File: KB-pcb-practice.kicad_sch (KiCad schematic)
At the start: 12 parts

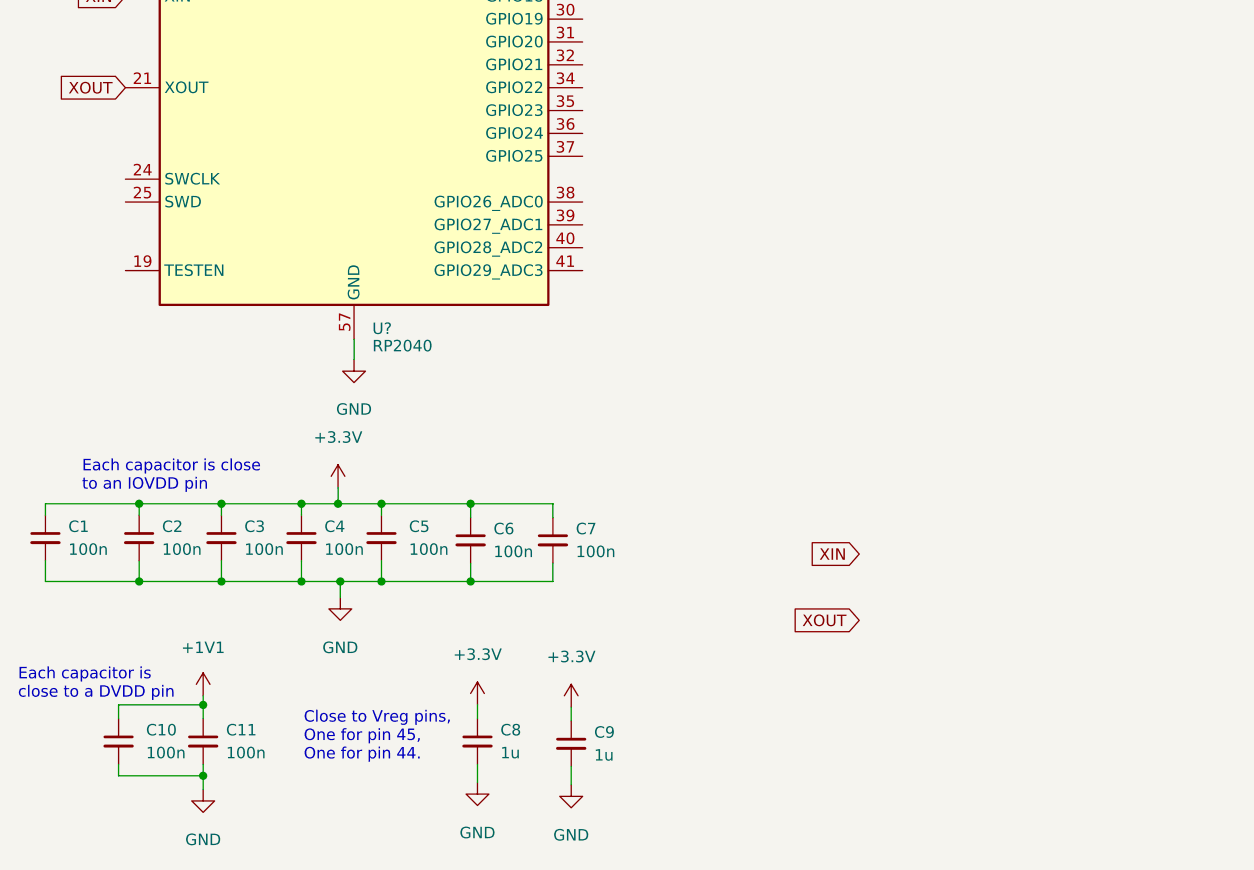
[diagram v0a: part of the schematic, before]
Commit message: Added Clock Circuit to Sch
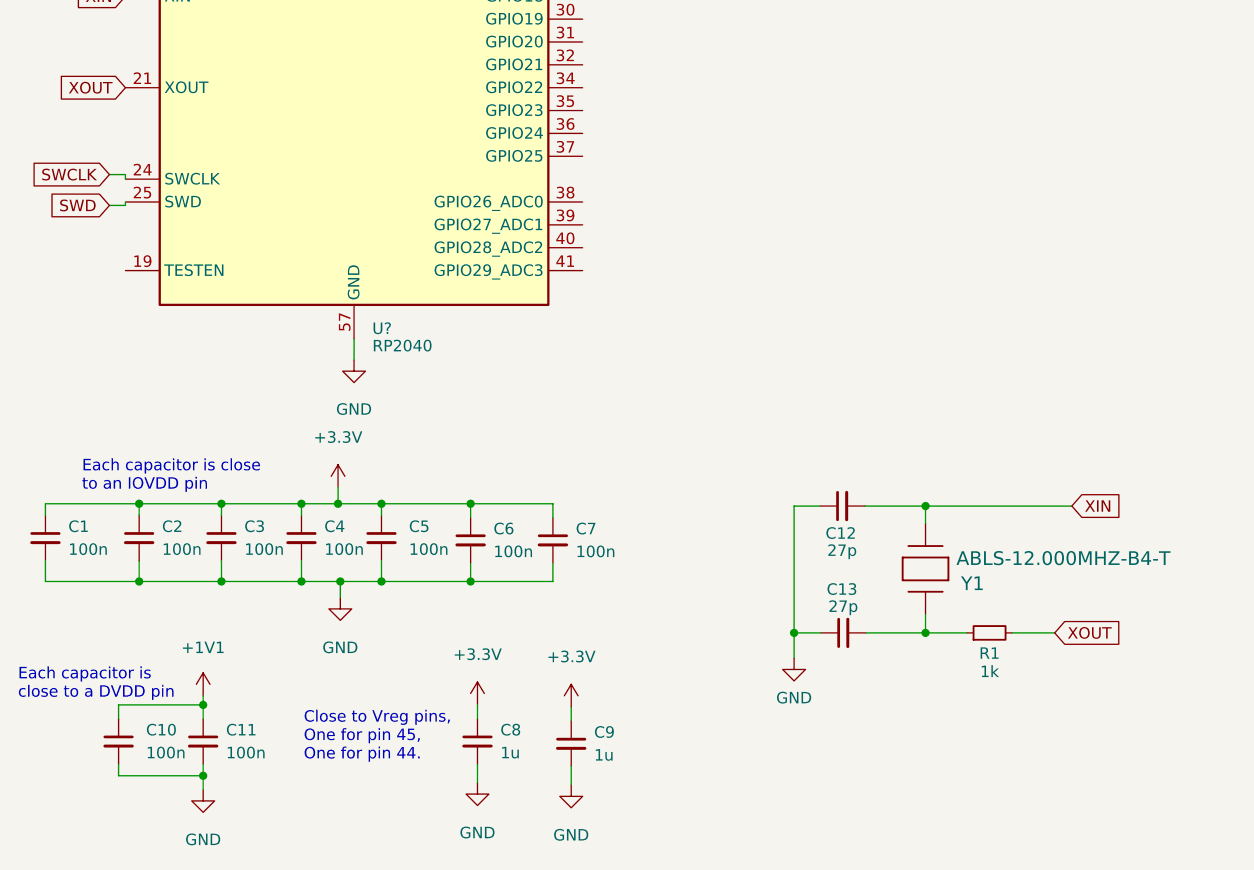
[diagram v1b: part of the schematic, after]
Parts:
- added C12, C13: 27p, symbol Device:C_Small
- added R1: 1k, symbol Device:R_Small
- added Y1: ABLS-12.000MHZ-B4-T, XTAL_ABLS_ABR, symbol ABLS-12MHZ-B4-T:ABLS-12.000MHZ-B4-T
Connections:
- net GND: now also C12.1, C13.1
- net XIN: now also C12.2, Y1.2
- net XOUT: now also R1.2
- net SWCLK: now reaches U?.24 (SWCLK)
- net SWD: now reaches U?.25 (SWD)
- new net: C13.2, R1.1, Y1.1
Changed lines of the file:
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@@
   (junction (at 33.274 155.702) (diameter 0) (color 0 0 0 0)
   )
+  (junction (at 113.538 133.604) (diameter 0) (color 0 0 0 0)
+  )
   (junction (at 35.306 141.986) (diameter 0) (color 0 0 0 0)
   )
+  (junction (at 98.933 147.701) (diameter 0) (color 0 0 0 0)
+  )
   (junction (at 44.196 141.986) (diameter 0) (color 0 0 0 0)
   )
   (junction (at 62.992 141.986) (diameter 0) (color 0 0 0 0)
   )
+  (junction (at 113.538 147.701) (diameter 0) (color 0 0 0 0)
+  )
   (wire (pts (xy 62.992 133.35) (xy 53.086 133.35))
     (stroke (width 0) (type default) (color 0 0 0 0))
@@
     (stroke (width 0) (type default) (color 0 0 0 0))
   )
+  (wire (pts (xy 24.638 99.822) (xy 24.638 100.203))
+    (stroke (width 0) (type default) (color 0 0 0 0))
+  )
   (wire (pts (xy 53.086 133.35) (xy 53.086 134.62))
     (stroke (width 0) (type default) (color 0 0 0 0))
   )
+  (wire (pts (xy 113.538 133.604) (xy 113.538 135.509))
+    (stroke (width 0) (type default) (color 0 0 0 0))
+  )
   (wire (pts (xy 44.196 141.986) (xy 44.196 139.7))
     (stroke (width 0) (type default) (color 0 0 0 0))
@@
     (stroke (width 0) (type default) (color 0 0 0 0))
   )
+  (wire (pts (xy 24.638 96.774) (xy 22.86 96.774))
+    (stroke (width 0) (type default) (color 0 0 0 0))
+  )
+  (wire (pts (xy 113.538 145.669) (xy 113.538 147.701))
+    (stroke (width 0) (type default) (color 0 0 0 0))
+  )
+  (wire (pts (xy 98.933 147.701) (xy 98.933 150.495))
+    (stroke (width 0) (type default) (color 0 0 0 0))
+  )
+  (wire (pts (xy 129.794 133.604) (xy 113.538 133.604))
+    (stroke (width 0) (type default) (color 0 0 0 0))
+  )
+  (wire (pts (xy 98.933 147.701) (xy 101.854 147.701))
+    (stroke (width 0) (type default) (color 0 0 0 0))
+  )
   (wire (pts (xy 23.876 163.576) (xy 33.274 163.576))
     (stroke (width 0) (type default) (color 0 0 0 0))
@@
     (stroke (width 0) (type default) (color 0 0 0 0))
   )
+  (wire (pts (xy 118.11 147.701) (xy 113.538 147.701))
+    (stroke (width 0) (type default) (color 0 0 0 0))
+  )
+  (wire (pts (xy 24.638 100.203) (xy 22.86 100.203))
+    (stroke (width 0) (type default) (color 0 0 0 0))
+  )
+  (wire (pts (xy 123.19 147.701) (xy 127.889 147.701))
+    (stroke (width 0) (type default) (color 0 0 0 0))
+  )
   (wire (pts (xy 44.196 134.62) (xy 44.196 133.35))
     (stroke (width 0) (type default) (color 0 0 0 0))
@@
     (stroke (width 0) (type default) (color 0 0 0 0))
   )
+  (wire (pts (xy 98.933 133.604) (xy 98.933 147.701))
+    (stroke (width 0) (type default) (color 0 0 0 0))
+  )
   (wire (pts (xy 48.26 133.35) (xy 53.086 133.35))
     (stroke (width 0) (type default) (color 0 0 0 0))
@@
     (stroke (width 0) (type default) (color 0 0 0 0))
   )
+  (wire (pts (xy 101.727 133.604) (xy 98.933 133.604))
+    (stroke (width 0) (type default) (color 0 0 0 0))
+  )
+  (wire (pts (xy 113.538 147.701) (xy 106.934 147.701))
+    (stroke (width 0) (type default) (color 0 0 0 0))
+  )
   (wire (pts (xy 44.196 141.986) (xy 35.306 141.986))
     (stroke (width 0) (type default) (color 0 0 0 0))
@@
     (stroke (width 0) (type default) (color 0 0 0 0))
   )
+  (wire (pts (xy 24.638 97.282) (xy 24.638 96.774))
+    (stroke (width 0) (type default) (color 0 0 0 0))
+  )
   (wire (pts (xy 26.162 134.62) (xy 26.162 133.35))
     (stroke (width 0) (type default) (color 0 0 0 0))
   )
   (wire (pts (xy 60.198 22.352) (xy 60.198 23.622))
+    (stroke (width 0) (type default) (color 0 0 0 0))
+  )
+  (wire (pts (xy 106.807 133.604) (xy 113.538 133.604))
     (stroke (width 0) (type default) (color 0 0 0 0))
   )
@@
     )
   )
-  (global_label "XIN" (shape input) (at 106.172 138.938 180) (fields_autoplaced)
-    (effects (font (size 1.27 1.27)) (justify right))
-    (property "Intersheet References" "${INTERSHEET_REFS}" (id 0) (at 100.6141 138.8586 0)
-      (effects (font (size 1.27 1.27)) (justify right) hide)
+  (global_label "XIN" (shape input) (at 129.794 133.604 0) (fields_autoplaced)
+    (effects (font (size 1.27 1.27)) (justify left))
+    (property "Intersheet References" "${INTERSHEET_REFS}" (id 0) (at 135.3519 133.5246 0)
+      (effects (font (size 1.27 1.27)) (justify left) hide)
     )
   )
@@
     )
   )
-  (global_label "XOUT" (shape input) (at 106.172 146.304 180) (fields_autoplaced)
+  (global_label "SWD" (shape input) (at 22.86 100.203 180) (fields_autoplaced)
     (effects (font (size 1.27 1.27)) (justify right))
-    (property "Intersheet References" "${INTERSHEET_REFS}" (id 0) (at 98.9208 146.2246 0)
+    (property "Intersheet References" "${INTERSHEET_REFS}" (id 0) (at 16.5159 100.1236 0)
+      (effects (font (size 1.27 1.27)) (justify right) hide)
+    )
+  )
+  (global_label "XOUT" (shape input) (at 127.889 147.701 0) (fields_autoplaced)
+    (effects (font (size 1.27 1.27)) (justify left))
+    (property "Intersheet References" "${INTERSHEET_REFS}" (id 0) (at 135.1402 147.6216 0)
+      (effects (font (size 1.27 1.27)) (justify left) hide)
+    )
+  )
+  (global_label "SWCLK" (shape input) (at 22.86 96.774 180) (fields_autoplaced)
+    (effects (font (size 1.27 1.27)) (justify right))
+    (property "Intersheet References" "${INTERSHEET_REFS}" (id 0) (at 14.2179 96.6946 0)
       (effects (font (size 1.27 1.27)) (justify right) hide)
     )
@@
     (pin "1")
   )
+  (symbol (lib_id "ABLS-12MHZ-B4-T:ABLS-12.000MHZ-B4-T") (at 113.538 145.669 90) (unit 1)
+    (in_bom yes) (on_board yes)
+    (property "Reference" "Y1" (id 0) (at 117.475 142.24 90)
+      (effects (font (size 1.524 1.524)) (justify right))
+    )
+    (property "Value" "ABLS-12.000MHZ-B4-T" (id 1) (at 116.967 139.446 90)
+      (effects (font (size 1.524 1.524)) (justify right))
+    )
+    (property "Footprint" "XTAL_ABLS_ABR" (id 2) (at 122.682 140.589 0)
+      (effects (font (size 1.524 1.524)) hide)
+    )
+    (property "Datasheet" "" (id 3) (at 113.538 145.669 0)
+      (effects (font (size 1.524 1.524)))
+    )
+    (pin "1")
+    (pin "2")
+  )
+  (symbol (lib_id "power:GND") (at 98.933 150.495 0) (unit 1)
+    (in_bom yes) (on_board yes) (fields_autoplaced)
+    (property "Reference" "#PWR?" (id 0) (at 98.933 156.845 0)
+      (effects (font (size 1.27 1.27)) hide)
+    )
+    (property "Value" "GND" (id 1) (at 98.933 154.94 0))
+    (property "Footprint" "" (id 2) (at 98.933 150.495 0)
+      (effects (font (size 1.27 1.27)) hide)
+    )
+    (property "Datasheet" "" (id 3) (at 98.933 150.495 0)
+      (effects (font (size 1.27 1.27)) hide)
+    )
+    (pin "1")
+  )
   (symbol (lib_id "power:GND") (at 33.274 165.1 0) (unit 1)
     (in_bom yes) (on_board yes) (fields_autoplaced)
@@
     (pin "2")
   )
+  (symbol (lib_id "Device:C_Small") (at 104.267 133.604 90) (unit 1)
+    (in_bom yes) (on_board yes)
+    (property "Reference" "C12" (id 0) (at 104.14 136.652 90))
+    (property "Value" "27p" (id 1) (at 104.267 138.557 90))
+    (property "Footprint" "" (id 2) (at 104.267 133.604 0)
+      (effects (font (size 1.27 1.27)) hide)
+    )
+    (property "Datasheet" "~" (id 3) (at 104.267 133.604 0)
+      (effects (font (size 1.27 1.27)) hide)
+    )
+    (pin "1")
+    (pin "2")
+  )
   (symbol (lib_id "Device:C_Small") (at 26.162 137.16 0) (unit 1)
     (in_bom yes) (on_board yes) (fields_autoplaced)
@@
     (pin "1")
   )
+  (symbol (lib_id "Device:R_Small") (at 120.65 147.701 90) (unit 1)
+    (in_bom yes) (on_board yes)
+    (property "Reference" "R1" (id 0) (at 120.65 149.987 90))
+    (property "Value" "1k" (id 1) (at 120.65 152.019 90))
+    (property "Footprint" "" (id 2) (at 120.65 147.701 0)
+      (effects (font (size 1.27 1.27)) hide)
+    )
+    (property "Datasheet" "~" (id 3) (at 120.65 147.701 0)
+      (effects (font (size 1.27 1.27)) hide)
+    )
+    (pin "1")
+    (pin "2")
+  )
   (symbol (lib_id "power:+1V1") (at 44.958 22.606 0) (unit 1)
     (in_bom yes) (on_board yes) (fields_autoplaced)
@@
     )
     (property "Datasheet" "~" (id 3) (at 35.306 137.16 0)
+      (effects (font (size 1.27 1.27)) hide)
+    )
+    (pin "1")
+    (pin "2")
+  )
+  (symbol (lib_id "Device:C_Small") (at 104.394 147.701 90) (unit 1)
+    (in_bom yes) (on_board yes)
+    (property "Reference" "C13" (id 0) (at 104.267 142.875 90))
+    (property "Value" "27p" (id 1) (at 104.394 144.78 90))
+    (property "Footprint" "" (id 2) (at 104.394 147.701 0)
+      (effects (font (size 1.27 1.27)) hide)
+    )
+    (property "Datasheet" "~" (id 3) (at 104.394 147.701 0)
       (effects (font (size 1.27 1.27)) hide)
     )
@@
       (reference "#PWR?") (unit 1) (value "GND") (footprint "")
     )
+    (path "/7690133a-81e0-41f0-9fb1-5ff9869e266d"
+      (reference "#PWR?") (unit 1) (value "GND") (footprint "")
+    )
     (path "/7a920f59-5109-41c4-a9f1-bac1ca825631"
       (reference "#PWR?") (unit 1) (value "GND") (footprint "")
@@
       (reference "C11") (unit 1) (value "100n") (footprint "")
     )
+    (path "/bc9d3f77-d1f1-420c-80e1-657e11335ca1"
+      (reference "C12") (unit 1) (value "27p") (footprint "")
+    )
+    (path "/d75311b5-5e6d-4e95-b883-053d4a8c1b43"
+      (reference "C13") (unit 1) (value "27p") (footprint "")
+    )
+    (path "/cccfb0b1-1795-48ba-9c3e-27ddb0efc39b"
+      (reference "R1") (unit 1) (value "1k") (footprint "")
+    )
     (path "/53b10514-b03b-4e0b-a965-148101e5a7b5"
       (reference "U?") (unit 1) (value "RP2040") (footprint "Package_DFN_QFN:QFN-56-1EP_7x7mm_P0.4mm_EP3.2x3.2mm")
     )
-  )
+    (path "/74351c43-ff9c-4a0b-b435-003e9a61fcaa"
+      (reference "Y1") (unit 1) (value "ABLS-12.000MHZ-B4-T") (footprint "XTAL_ABLS_ABR")
+    )
+  )

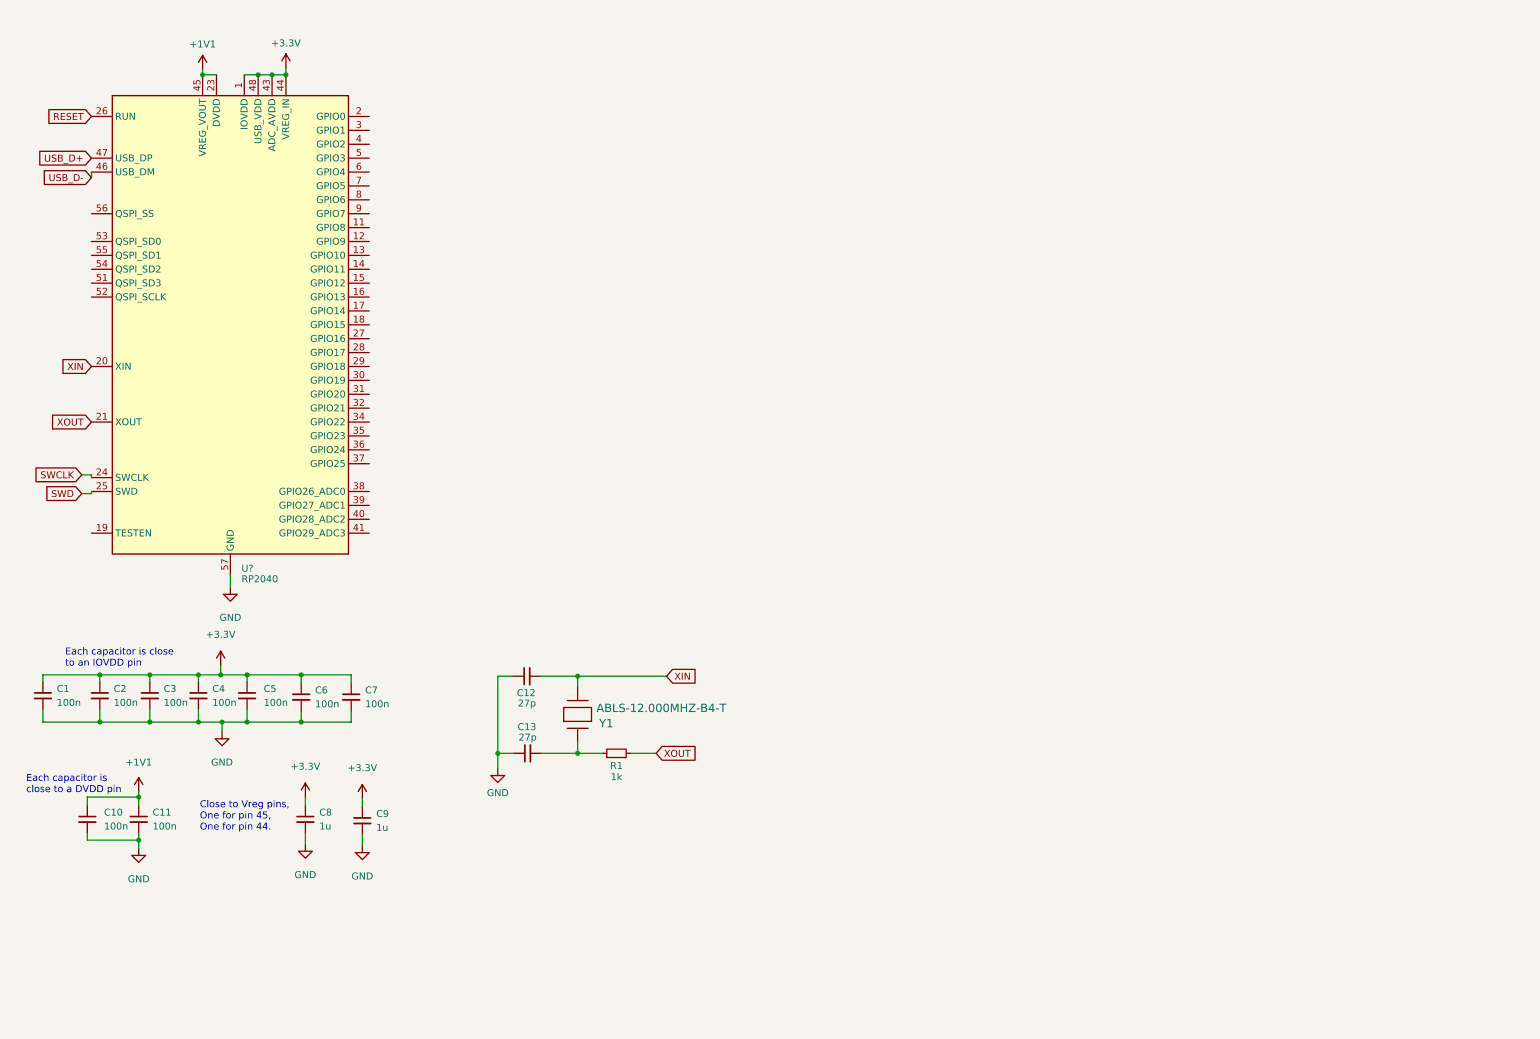
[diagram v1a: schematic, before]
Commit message: Added reset circuit and Quad SPI Flash
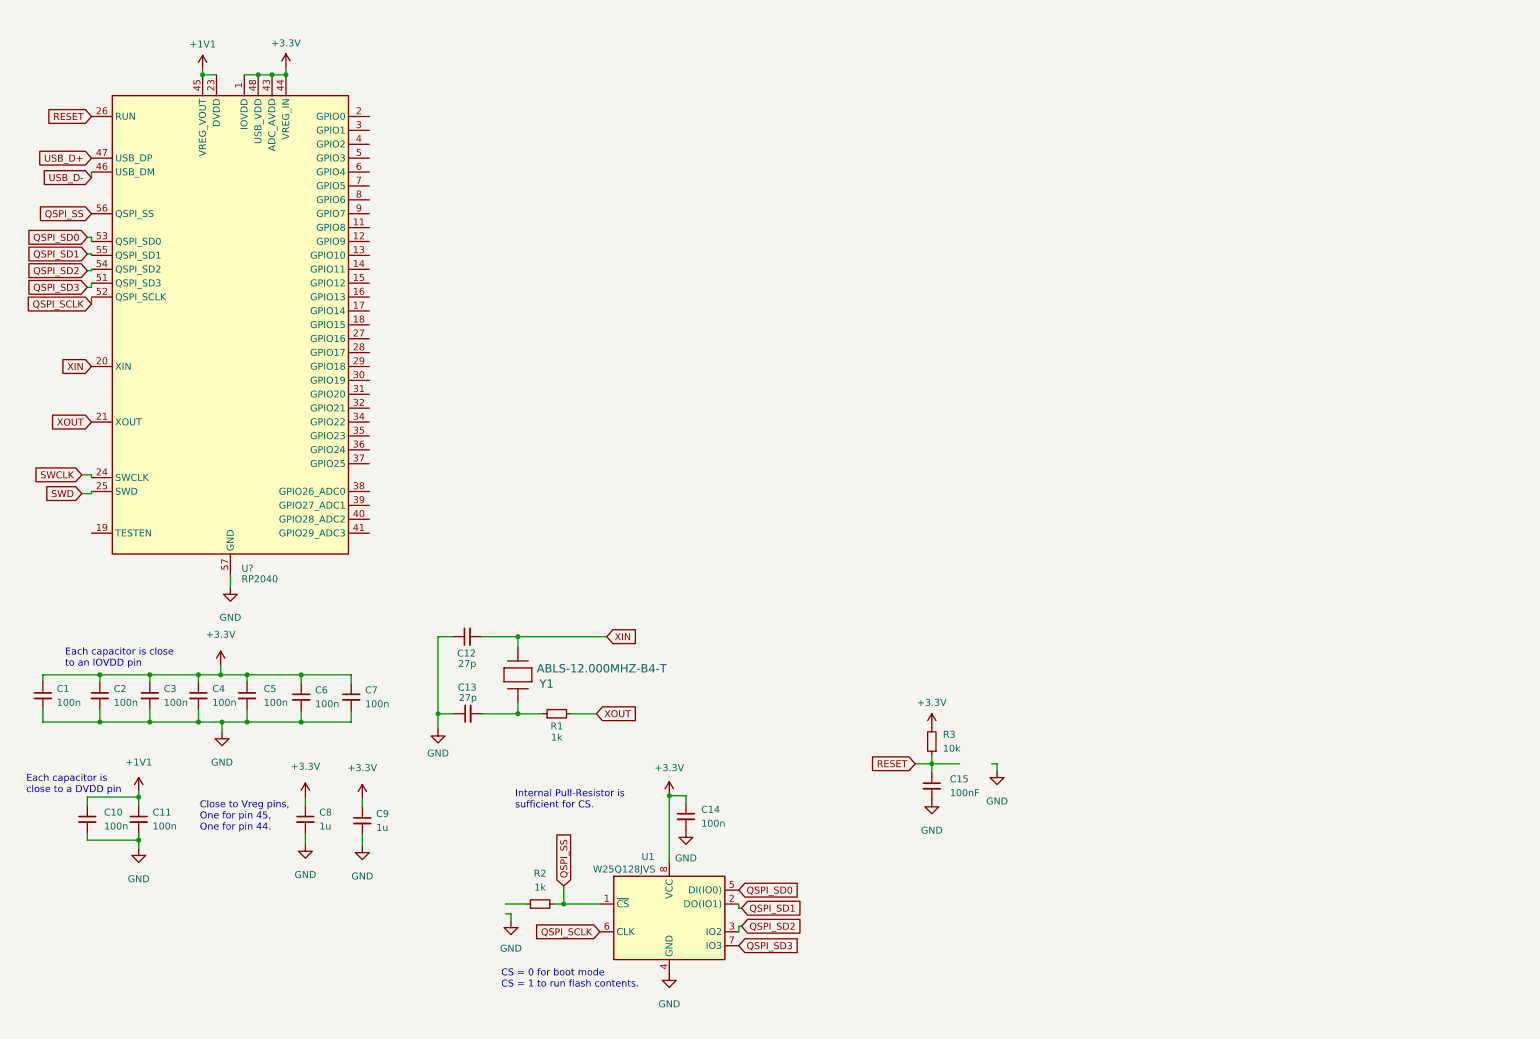
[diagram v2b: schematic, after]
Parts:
- added C14: 100n, symbol Device:C_Small
- added C15: 100nF, symbol Device:C_Small
- added R2: 1k, symbol Device:R_Small
- added R3: 10k, symbol Device:R_Small
- added U1: W25Q128JVS, Package_SO:SOIC-8_5.23x5.23mm_P1.27mm, symbol Memory_Flash:W25Q128JVS
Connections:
- net +3.3V: now also C14.1, R3.2, U1.8 (VCC)
- net GND: now also C14.2, C15.2, U1.4 (GND)
- net RESET: now also C15.1, R3.1
- net QSPI_SD3: now reaches U?.51 (QSPI_SD3)
- net QSPI_SD3: now also U1.7 (IO3)
- net QSPI_SCLK: now reaches U?.52 (QSPI_SCLK)
- net QSPI_SCLK: now also U1.6 (CLK)
- net QSPI_SD0: now reaches U?.53 (QSPI_SD0)
- net QSPI_SD0: now also U1.5 (DI(IO0))
- net QSPI_SD2: now reaches U?.54 (QSPI_SD2)
- net QSPI_SD2: now also U1.3 (IO2)
- net QSPI_SD1: now reaches U?.55 (QSPI_SD1)
- net QSPI_SD1: now also U1.2 (DO(IO1))
- net QSPI_SS: now reaches U?.56 (QSPI_SS)
- net QSPI_SS: now also R2.2, U1.1 (~{CS})
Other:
- note added: "CS = 0 for boot mode CS = 1 to run flash contents."
- note added: "Internal Pull-Resistor is sufficient for CS."
- moved on the sheet: C12, C13, R1, Y1
